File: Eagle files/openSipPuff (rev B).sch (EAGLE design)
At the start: 20 parts, among them J2 1X04-RA, J3 AVR_SPI_PRG_62X3_LOCK, U1 ATMEGA32U4TQFP, U2 AD8223, U3 MPX12GP, Y1 16MHz

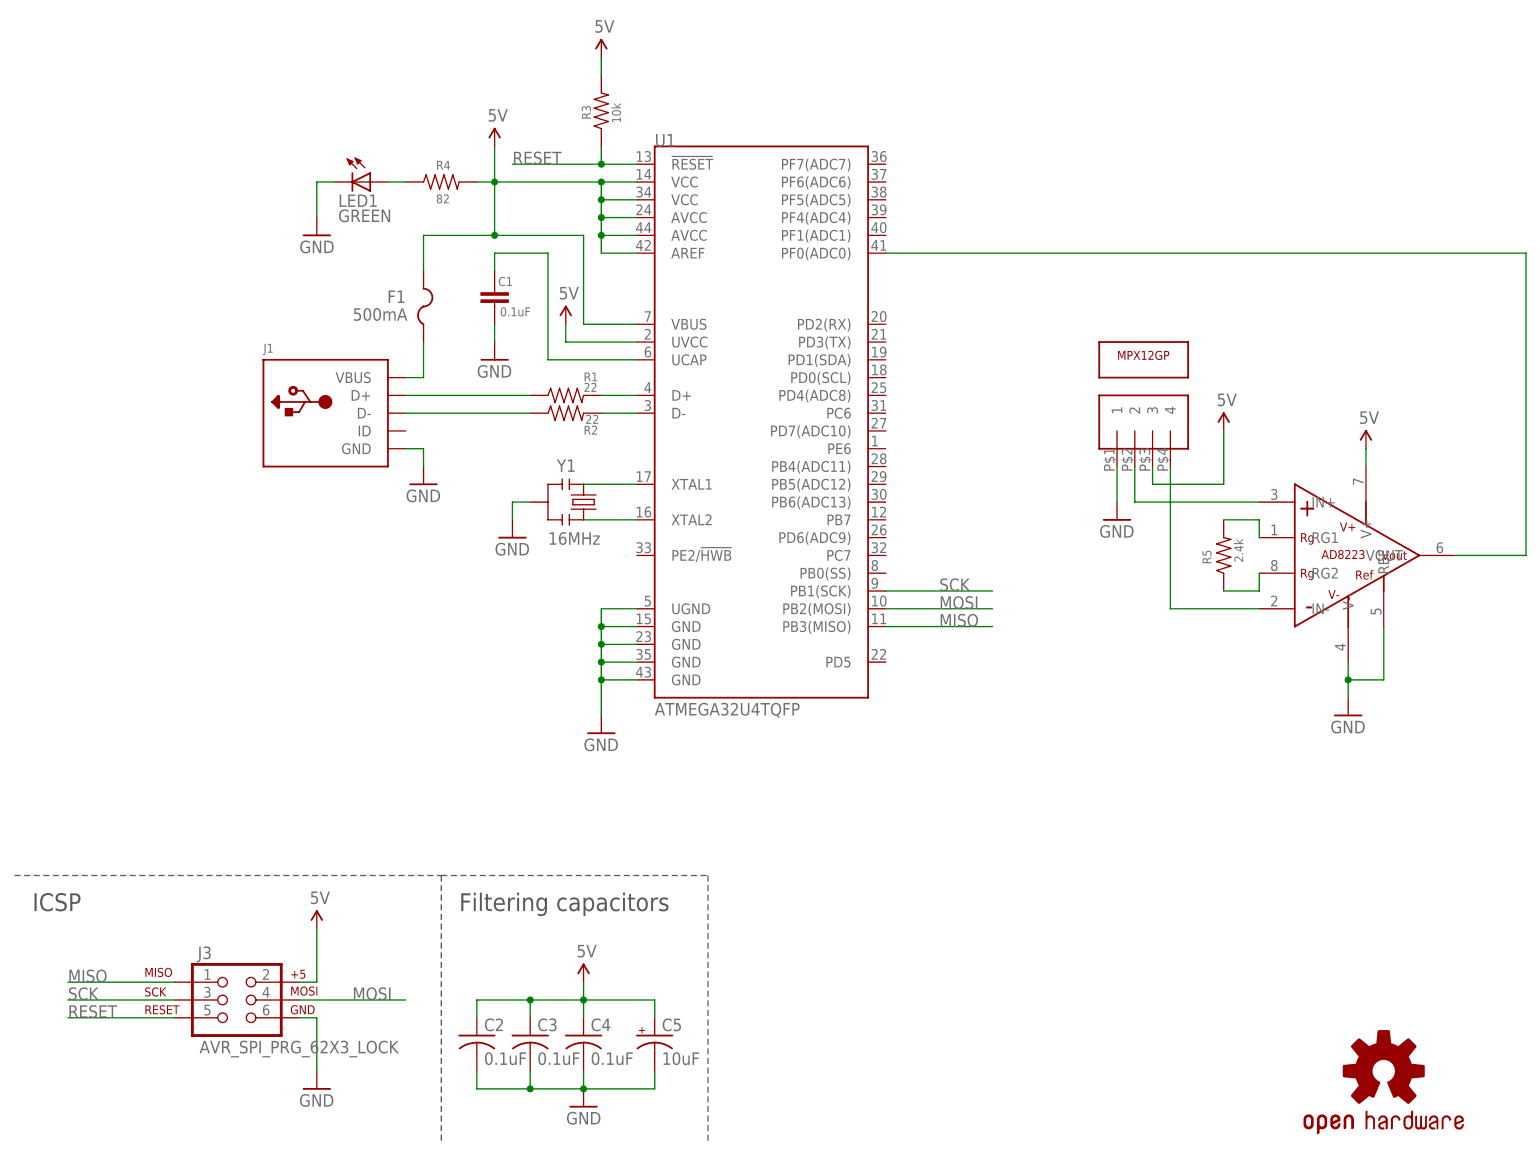
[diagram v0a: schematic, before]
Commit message: Firmware update and rev B Eagle files
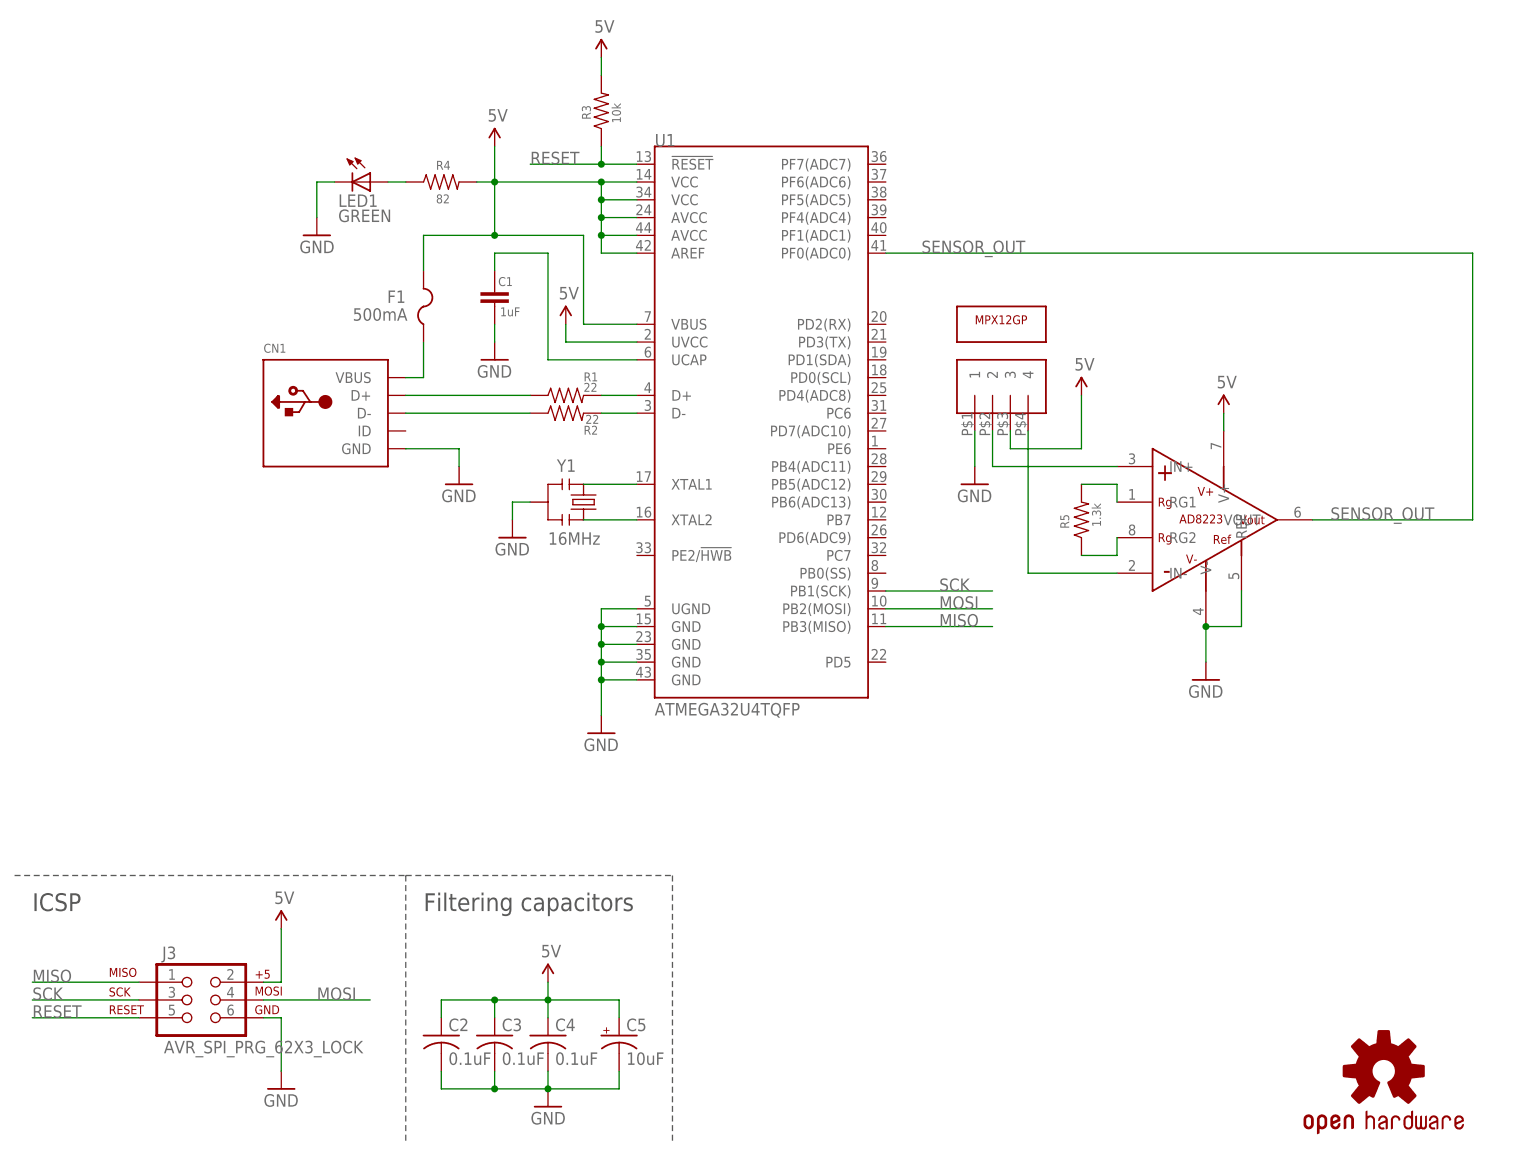
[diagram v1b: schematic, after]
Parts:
- removed J1: (no value), adafruit:USBMINIB
- added CN1: (no value), adafruit:USBMOLEX
- C1: value 0.1uF -> 1uF
- LOGO1: value OSHW-LOGOL -> OSHW-LOGOM; device SparkFun-Aesthetics:OSHW-LOGOL -> SparkFun-Aesthetics:OSHW-LOGOM
- R5: value 2.4k -> 1.3k
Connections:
- net OUTPUT renamed SENSOR_OUT
- removed net N$8: J1.D+, R1.1
- removed net N$9: J1.D-, R2.1
- new net D+: CN1.D+, R1.1
- new net D-: CN1.D-, R2.1
- net GND: now also CN1.GND; no longer J1.GND
- net N$4: now also CN1.VBUS; no longer J1.VBUS
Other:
- moved on the sheet: C2, C3, C4, C5, J3, R5
